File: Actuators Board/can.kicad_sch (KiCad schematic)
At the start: 1 part, among them U4 SN65HVD230

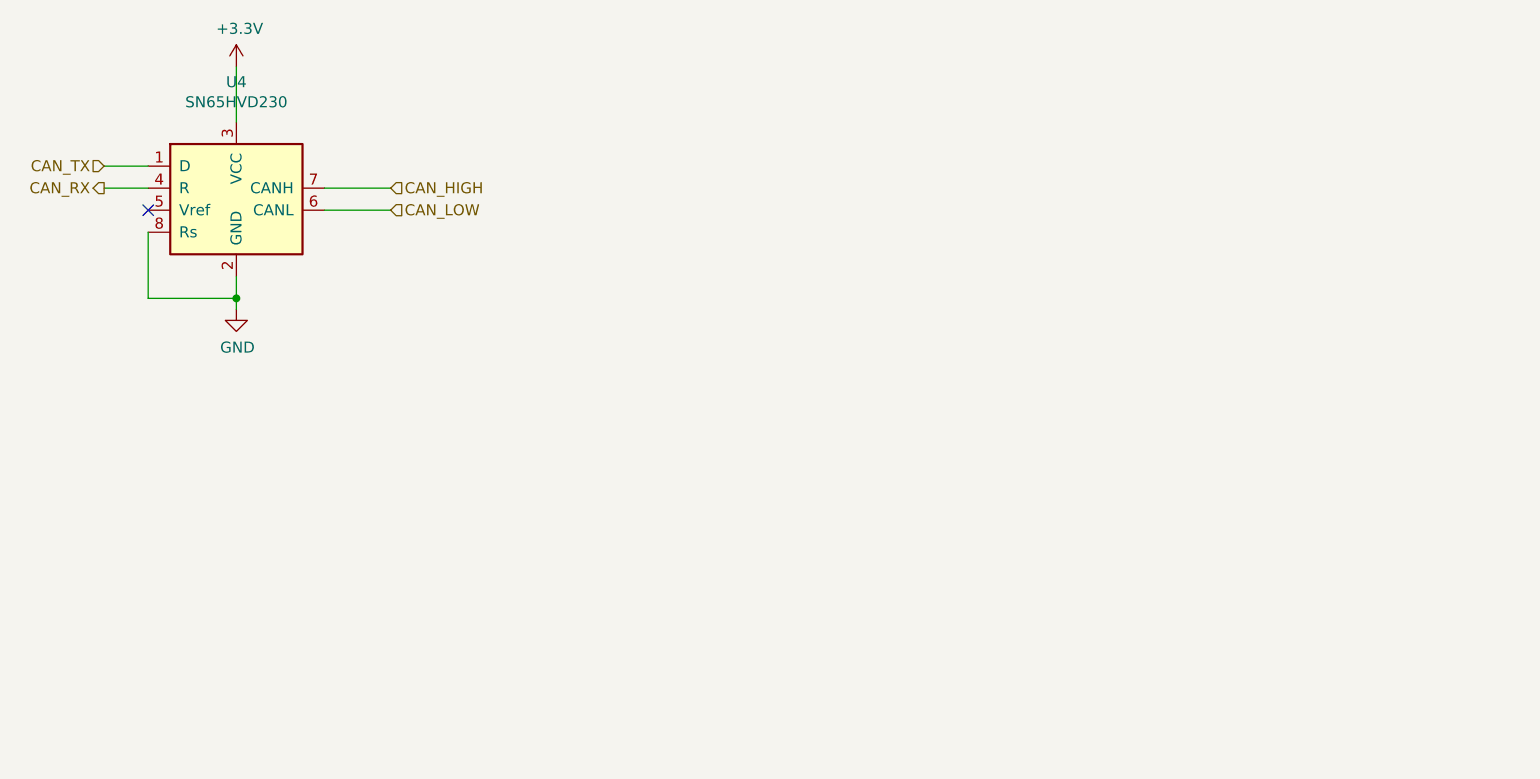
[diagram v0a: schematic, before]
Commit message: Added schematic for CAN transceiver passives; Deleted unused files
Values still need to be assigned
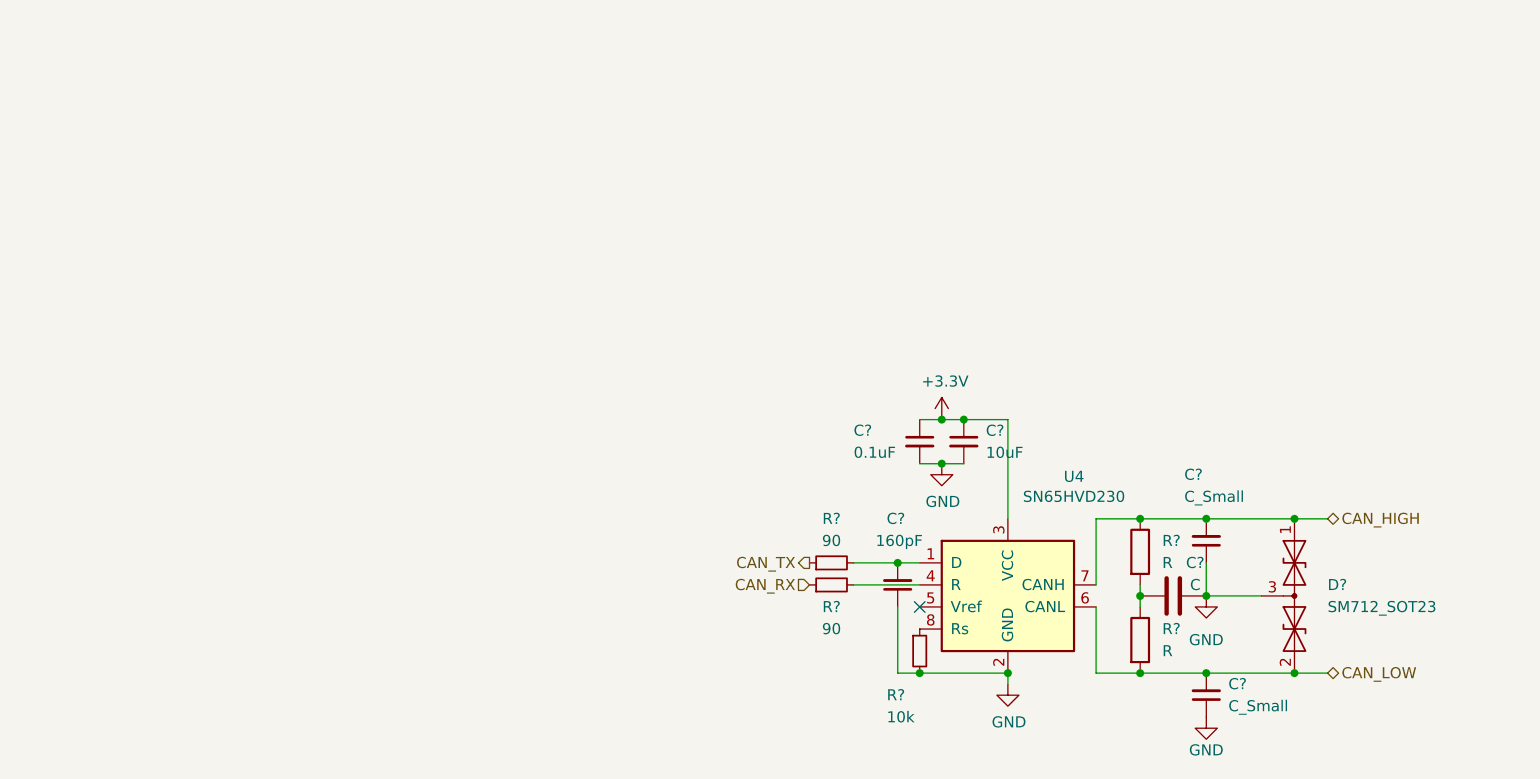
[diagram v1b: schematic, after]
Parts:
- added C?: 10uF, symbol Device:C_Small
- added C? (x2): C_Small, symbol Device:C_Small
- added C?: 160pF, symbol Device:C_Small
- added C?: 0.1uF, symbol Device:C_Small
- added C?: C, symbol Device:C
- added D?: SM712_SOT23, Package_TO_SOT_SMD:SOT-23, symbol Diode:SM712_SOT23
- added R? (x2): 90, symbol Device:R_Small
- added R?: 10k, symbol Device:R_Small
- added R? (x2): R, symbol Device:R
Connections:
- net +3V3: now also C?.1, C?.1
- net CAN_HIGH: now also C?.2, D?.1 (A1), R?.1
- net CAN_LOW: now also C?.2, D?.2 (A2), R?.2
- net CAN_RX: now also R?.1; no longer U4.4 (R)
- net CAN_TX: now also R?.1; no longer U4.1 (D)
- net GND: now also C?.1, C?.1, C?.1, C?.2, C?.2, C?.2, D?.3 (common), R?.2; no longer U4.8 (Rs)
- new net: C?.2, R?.2, U4.1 (D)
- new net: R?.2, U4.4 (R)
- new net: R?.1, U4.8 (Rs)
- new net: C?.1, R?.1, R?.2
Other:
- moved on the sheet: U4

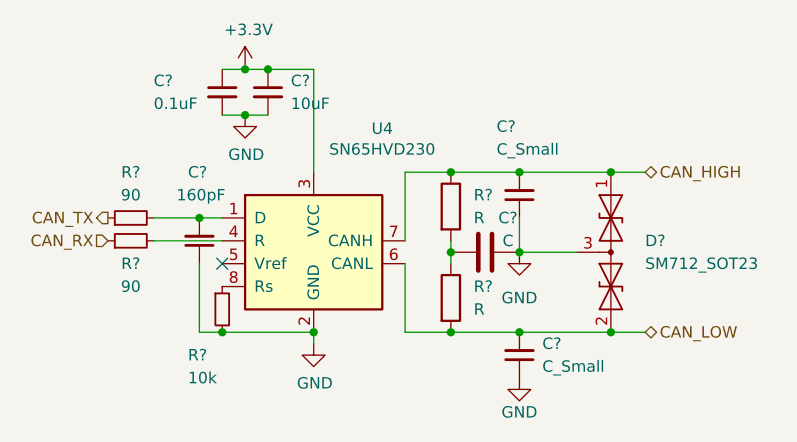
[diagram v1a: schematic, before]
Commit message: Assigned values to CAN passives, connected SSR GPIO
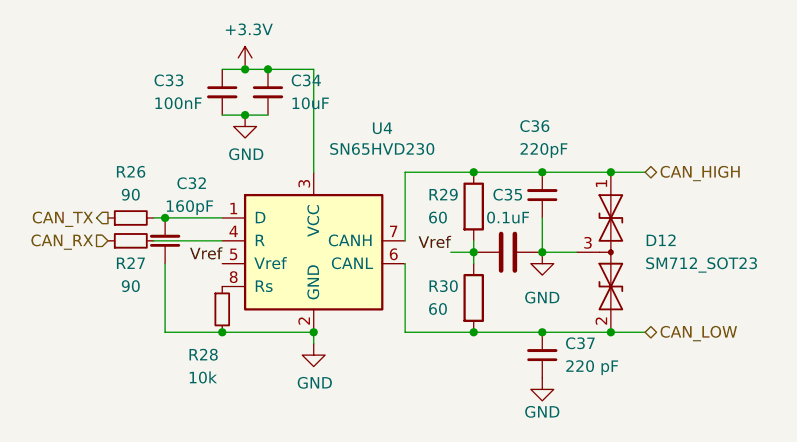
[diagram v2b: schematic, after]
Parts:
- C33: renamed from C?; value 0.1uF -> 100nF
- C35: renamed from C?; value C -> 0.1uF
- C36: renamed from C?; value C_Small -> 220pF
- C37: renamed from C?; value C_Small -> 220 pF
- R29, R30: renamed from R?; value R -> 60
- gave numbers to parts that had none: 6
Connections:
- net Vref: now reaches U4.5 (Vref)
- net Vref: now also C35.1, R29.2, R30.1
- no-connect marks 1 -> 0
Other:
- moved on the sheet: C32, C35, C36, C37, R29, R30

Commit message: Added solder jumpers and resistors for SSR pull-up and pull-down.
Also footprint assignment
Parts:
- C32, C33, C34, C35, C36, C37: footprint (none) -> Capacitor_SMD:C_0603_1608Metric
- R26, R27, R28: footprint (none) -> Resistor_SMD:R_0603_1608Metric
- R29, R30: footprint (none) -> Resistor_SMD:R_0805_2012Metric
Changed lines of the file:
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@@
       (effects (font (size 1.27 1.27)) (justify left))
     )
-    (property "Footprint" "" (id 2) (at 129.54 71.12 0)
+    (property "Footprint" "Capacitor_SMD:C_0603_1608Metric" (id 2) (at 129.54 71.12 0)
       (effects (font (size 1.27 1.27)) hide)
     )
@@
       (effects (font (size 1.27 1.27)) (justify right))
     )
-    (property "Footprint" "" (id 2) (at 160.02 82.55 0)
+    (property "Footprint" "Capacitor_SMD:C_0603_1608Metric" (id 2) (at 160.02 82.55 0)
       (effects (font (size 1.27 1.27)) hide)
     )
@@
       (effects (font (size 1.27 1.27)) (justify right))
     )
-    (property "Footprint" "" (id 2) (at 118.11 87.63 0)
+    (property "Footprint" "Capacitor_SMD:C_0603_1608Metric" (id 2) (at 118.11 87.63 0)
       (effects (font (size 1.27 1.27)) hide)
     )
@@
     (property "Reference" "R27" (id 0) (at 114.3 90.17 90))
     (property "Value" "90" (id 1) (at 114.3 92.71 90))
-    (property "Footprint" "" (id 2) (at 114.3 87.63 0)
+    (property "Footprint" "Resistor_SMD:R_0603_1608Metric" (id 2) (at 114.3 87.63 0)
       (effects (font (size 1.27 1.27)) hide)
     )
@@
     (property "Reference" "R26" (id 0) (at 114.3 80.01 90))
     (property "Value" "90" (id 1) (at 114.3 82.55 90))
-    (property "Footprint" "" (id 2) (at 114.3 85.09 0)
+    (property "Footprint" "Resistor_SMD:R_0603_1608Metric" (id 2) (at 114.3 85.09 0)
       (effects (font (size 1.27 1.27)) hide)
     )
@@
       (effects (font (size 1.27 1.27)) (justify left))
     )
-    (property "Footprint" "" (id 2) (at 124.46 71.12 0)
+    (property "Footprint" "Capacitor_SMD:C_0603_1608Metric" (id 2) (at 124.46 71.12 0)
       (effects (font (size 1.27 1.27)) hide)
     )
@@
       (effects (font (size 1.27 1.27)) (justify left))
     )
-    (property "Footprint" "" (id 2) (at 124.46 95.25 0)
+    (property "Footprint" "Resistor_SMD:R_0603_1608Metric" (id 2) (at 124.46 95.25 0)
       (effects (font (size 1.27 1.27)) hide)
     )
@@
       (effects (font (size 1.27 1.27)) (justify left))
     )
-    (property "Footprint" "" (id 2) (at 150.622 93.98 90)
+    (property "Footprint" "Resistor_SMD:R_0805_2012Metric" (id 2) (at 150.622 93.98 90)
       (effects (font (size 1.27 1.27)) hide)
     )
@@
       (effects (font (size 1.27 1.27)) (justify left))
     )
-    (property "Footprint" "" (id 2) (at 150.622 83.82 90)
+    (property "Footprint" "Resistor_SMD:R_0805_2012Metric" (id 2) (at 150.622 83.82 90)
       (effects (font (size 1.27 1.27)) hide)
     )
@@
     (property "Reference" "C35" (id 0) (at 156.21 82.55 90))
     (property "Value" "0.1uF" (id 1) (at 156.21 85.09 90))
-    (property "Footprint" "" (id 2) (at 160.02 87.9348 0)
+    (property "Footprint" "Capacitor_SMD:C_0603_1608Metric" (id 2) (at 160.02 87.9348 0)
       (effects (font (size 1.27 1.27)) hide)
     )
@@
       (effects (font (size 1.27 1.27)) (justify right))
     )
-    (property "Footprint" "" (id 2) (at 160.02 100.33 0)
-      (effects (font (size 1.27 1.27)) hide)
-    )
+    (property "Footprint" "Capacitor_SMD:C_0603_1608Metric" (id 2) (at 160.02 100.33 0)
+      (effects (font (size 1.27 1.27)) hide)
+    )

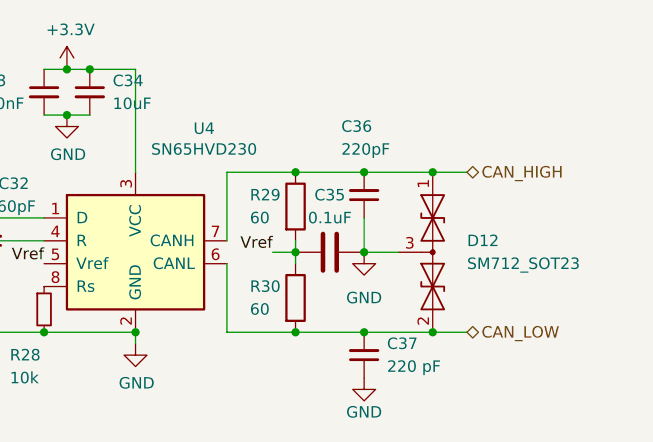
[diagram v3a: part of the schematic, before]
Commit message: Added solder jumper for CAN Vref
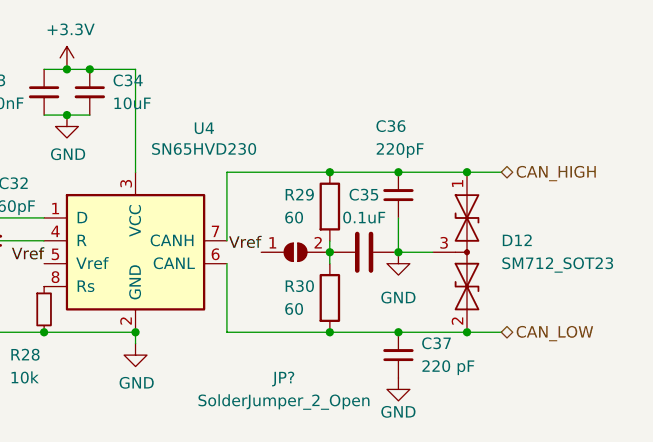
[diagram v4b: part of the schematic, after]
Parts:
- added JP?: SolderJumper_2_Open, symbol Jumper:SolderJumper_2_Open
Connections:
- net Vref: now also JP?.1 (A); no longer C35.1, R29.2, R30.1
- new net: C35.1, JP?.2 (B), R29.2, R30.1
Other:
- moved on the sheet: C35, C36, C37, D12, R29, R30

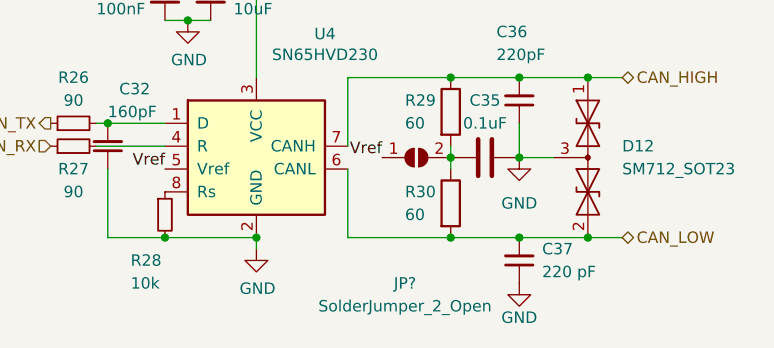
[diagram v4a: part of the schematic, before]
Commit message: Swapped RBUS connector, layout needs update.
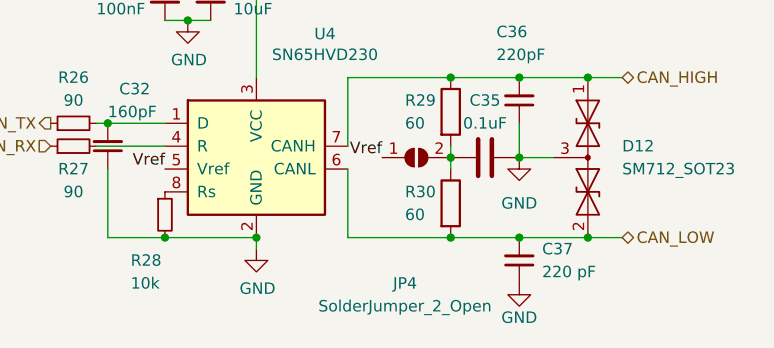
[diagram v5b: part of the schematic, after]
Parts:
- JP4: renamed from JP?; footprint (none) -> Jumper:SolderJumper-2_P1.3mm_Open_Pad1.0x1.5mm
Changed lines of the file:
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@@
   (symbol (lib_id "Jumper:SolderJumper_2_Open") (at 152.4 88.9 0) (unit 1)
     (in_bom yes) (on_board yes)
-    (property "Reference" "JP?" (id 0) (at 151.13 102.87 0))
+    (property "Reference" "JP4" (id 0) (at 151.13 102.87 0))
     (property "Value" "SolderJumper_2_Open" (id 1) (at 151.13 105.41 0))
-    (property "Footprint" "" (id 2) (at 152.4 88.9 0)
+    (property "Footprint" "Jumper:SolderJumper-2_P1.3mm_Open_Pad1.0x1.5mm" (id 2) (at 152.4 88.9 0)
       (effects (font (size 1.27 1.27)) hide)
     )
